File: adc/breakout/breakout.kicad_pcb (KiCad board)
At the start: 2 copper layers, 52 parts, among them J1 Conn_01x05_Pin, J2 Conn_01x05_Pin, J3 Conn_01x03_Pin, J4 Conn_01x06_Pin, U1 ESD5344D-TP, U2 ADS1261IRHBR, U3 ESD5344D-TP, U4 ESD5344D-TP

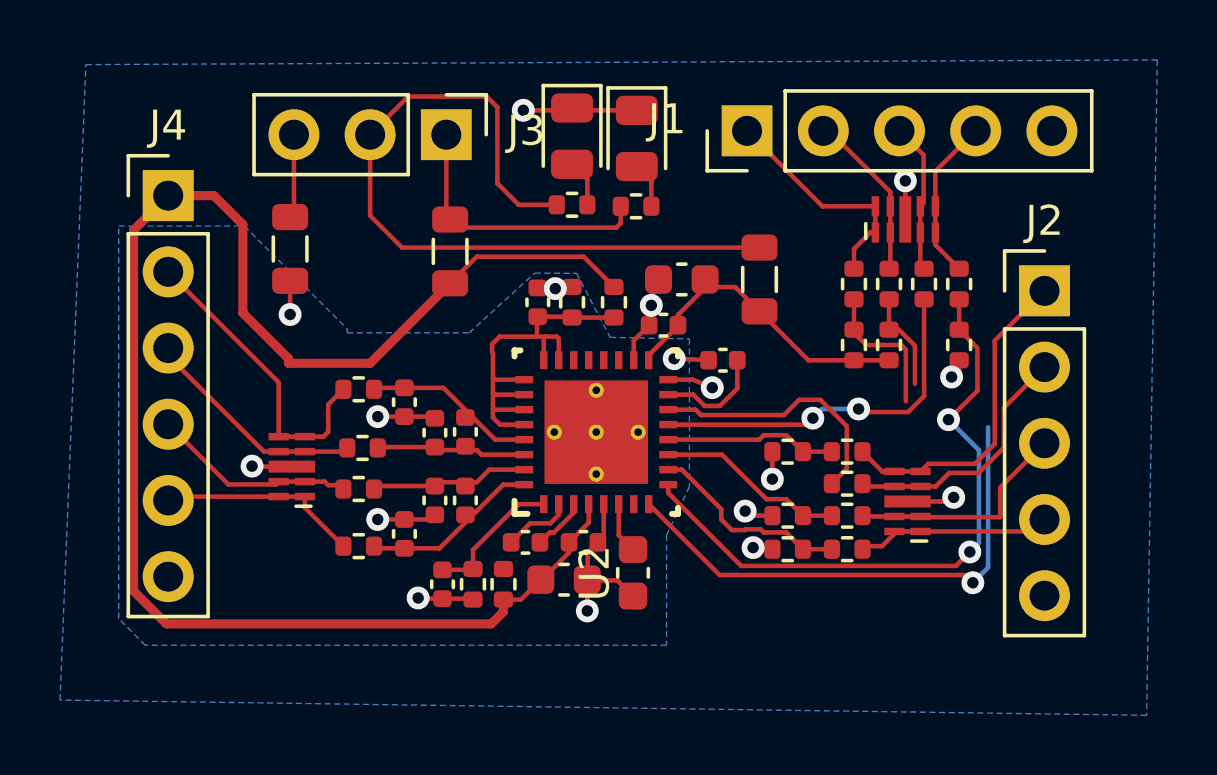
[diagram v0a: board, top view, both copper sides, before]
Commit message: More adc breakout pcb layout cleanup.
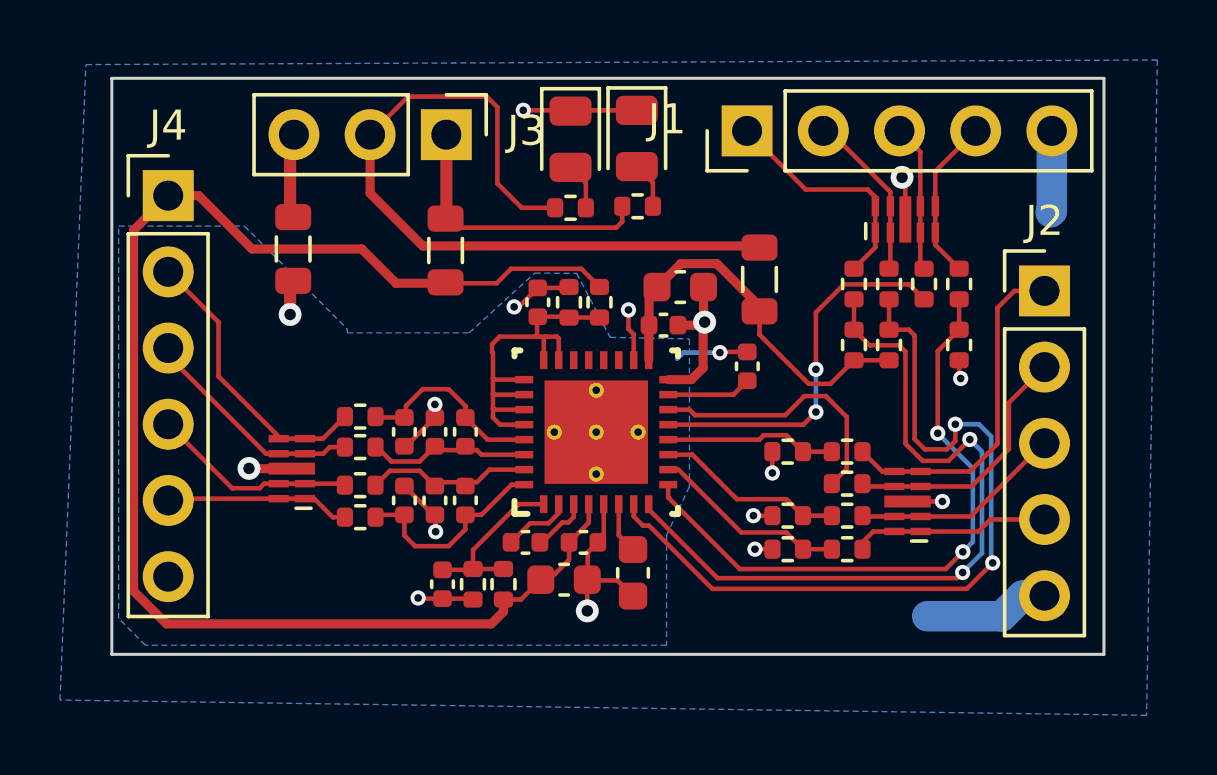
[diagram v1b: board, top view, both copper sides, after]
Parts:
- moved C14 1.11 mm to (113.8, 103.6)
- moved C9 0.99 mm to (113.8, 101.3)
- moved R30 0.97 mm to (112.3, 104.2)
- moved R26 0.91 mm to (112.3, 100.8)
- moved C7 0.84 mm to (125.2, 99.2), turned to 90 degrees
- moved R1 0.48 mm to (120.3, 97.0)
- moved C2 0.26 mm to (123.0, 96.5), turned to 0 degrees
- moved FB3 0.16 mm to (115.2, 95.3)
- moved R29 0.14 mm to (112.3, 103.1)
- moved D2 0.12 mm to (119.3, 91.6)
- moved R22 0.11 mm to (119.3, 93.9)
- moved R3 0.10 mm to (119.3, 97.0)
- moved FB1 0.10 mm to (110.1, 95.2)
- moved R28 0.08 mm to (112.3, 101.9)
- moved U4 0.07 mm to (110.0, 102.6)
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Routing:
- net Net-(U2-PWDN_N): track 3.37 -> 26.9 mm, vias 0 -> 2
- net GNDD: track 17.1 -> 25.3 mm
- net +5VA: track 52.6 -> 47.9 mm
- net Net-(U2-RESET_N): track 22.1 -> 25.3 mm, vias 1 -> 2
- net +3V3: track 10.4 -> 13.1 mm
- net GNDA: track 16.4 -> 17.8 mm
- net /AIN0: track 5.92 -> 6.96 mm
- net Net-(U2-AINCOM): track 4.66 -> 5.67 mm
- net /IN3: track 10.4 -> 9.53 mm
- net Net-(U2-BYPASS): track 3.64 -> 2.83 mm
- net /AIN3: track 5.74 -> 6.51 mm
- net /IN0: track 6.79 -> 6.09 mm
- net Net-(J2-Pin_1): track 10.9 -> 11.5 mm
- net Net-(J2-Pin_2): track 9.27 -> 8.66 mm
- net Net-(J2-Pin_3): track 7.69 -> 7.09 mm
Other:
- board outline added: 33.1 x 19.2 mm

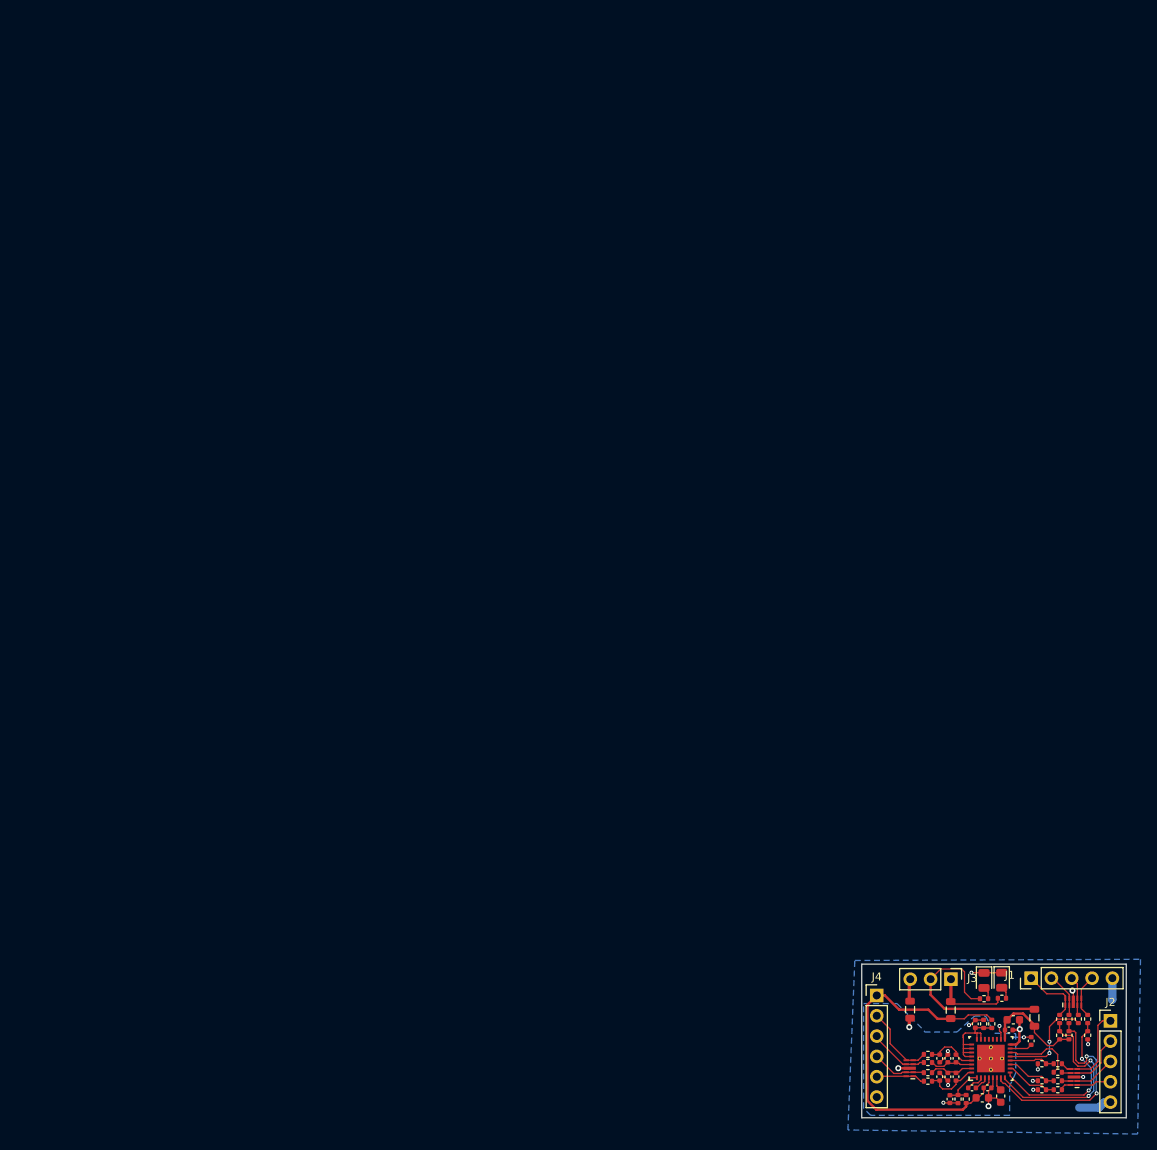
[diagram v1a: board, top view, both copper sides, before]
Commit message: Complete the adc breakout board layout.
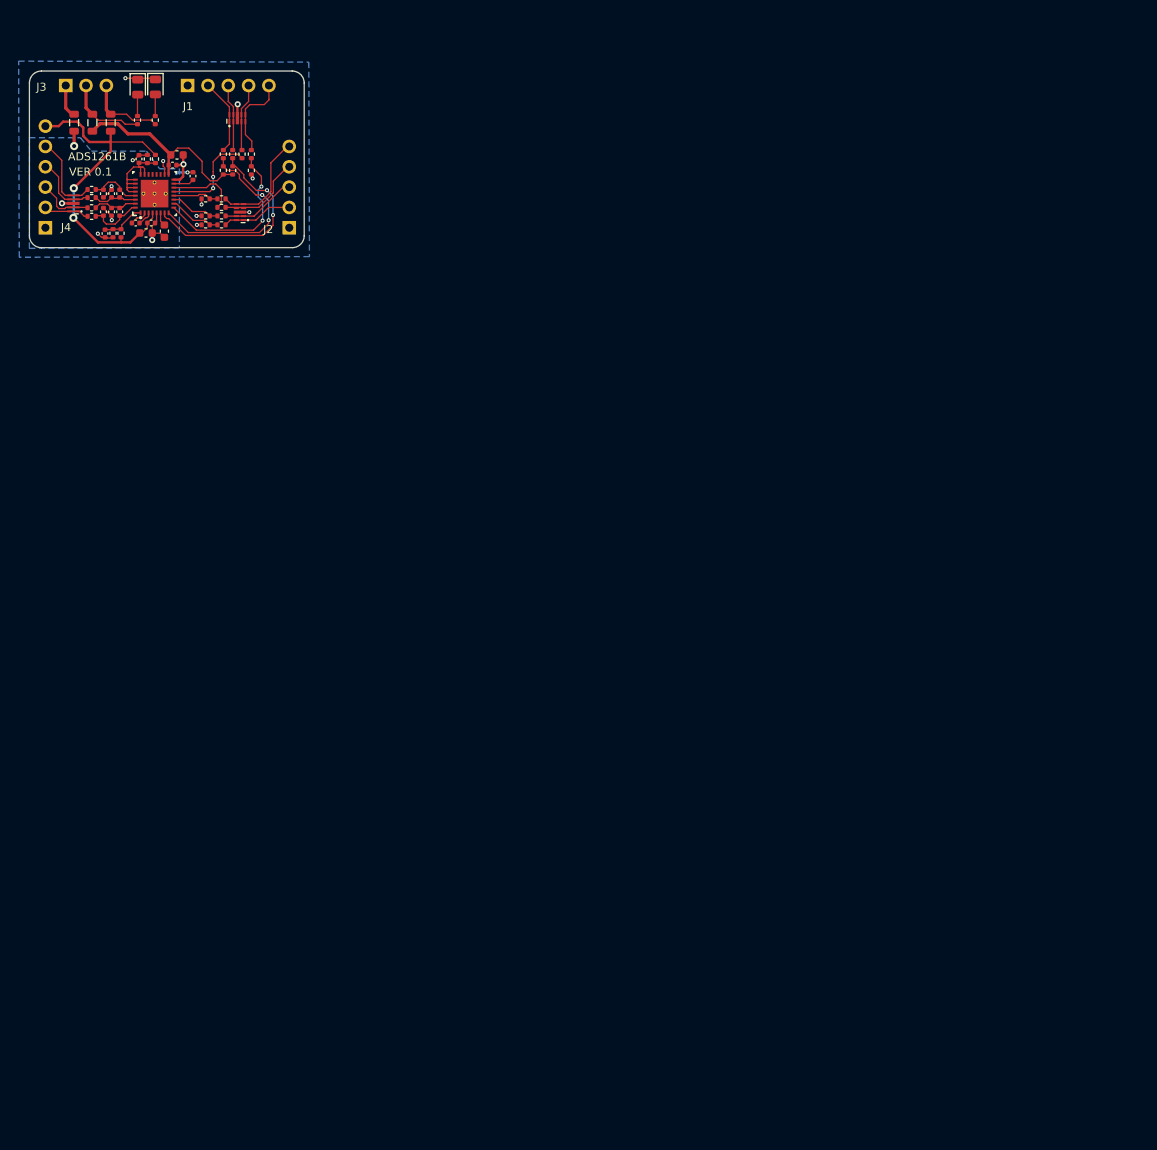
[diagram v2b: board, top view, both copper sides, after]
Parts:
- J1, J2: footprint Connector_PinHeader_2.54mm:PinHeader_1x05_P2.54mm_Vertical -> breakout:PinHeader_1x05_P2.54mm_Vertical
- J3: footprint Connector_PinHeader_2.54mm:PinHeader_1x03_P2.54mm_Vertical -> breakout:PinHeader_1x03_P2.54mm_Vertical
- J4: footprint Connector_PinHeader_2.54mm:PinHeader_1x06_P2.54mm_Vertical -> breakout:PinHeader_1x06_P2.54mm_Vertical
- moved FB2 162.4 mm to (7.87, -15.6)
- moved J3 157.2 mm to (4.54, -20.3), turned to 90 degrees
- moved D1 153.8 mm to (15.8, -20.1)
- moved D2 153.8 mm to (13.5, -20.1)
- moved J1 153.5 mm to (19.8, -20.3)
- moved FB3 152.7 mm to (10.2, -15.6)
- moved R22 152.5 mm to (13.5, -15.9), turned to 90 degrees
- moved R21 152.5 mm to (15.7, -15.9), turned to 90 degrees
- moved FB1 152.4 mm to (5.59, -15.6)
- moved U1 152.0 mm to (26.0, -16.2)
- moved R2 151.2 mm to (11.4, -1.80)
- moved R6 151.2 mm to (10.4, -1.80)
- moved C15 151.2 mm to (9.45, -1.77)
- moved C7 150.6 mm to (20.4, -8.95)
- moved C1 150.4 mm to (14.6, -1.84)
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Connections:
- J1 pad 1: Net-(J1-Pin_1) -> GNDD
- J1 pad 5: GNDD -> Net-(J1-Pin_5)
- J2 pad 1: Net-(J2-Pin_1) -> GNDD
- J2 pad 5: GNDD -> Net-(J2-Pin_5)
- J3 pad 1: /5V_LED -> GNDD
- J3 pad 3: GNDD -> /5V_LED
- J4 pad 1: +5VA -> GNDA
- J4 pad 2: /IN3 -> /IN0
- J4 pad 3: /IN2 -> /IN1
- J4 pad 4: /IN1 -> /IN2
- J4 pad 5: /IN0 -> /IN3
- J4 pad 6: GNDA -> +5VA
- R10 pad 1: Net-(J1-Pin_2) -> Net-(J1-Pin_3)
- R12 pad 1: Net-(J1-Pin_3) -> Net-(J1-Pin_4)
- R14 pad 1: Net-(J1-Pin_4) -> Net-(J1-Pin_5)
- R17 pad 1: Net-(J2-Pin_1) -> Net-(J2-Pin_5)
- R18 pad 1: Net-(J2-Pin_2) -> Net-(J2-Pin_4)
- R20 pad 1: Net-(J2-Pin_4) -> Net-(J2-Pin_2)
- R8 pad 1: Net-(J1-Pin_1) -> Net-(J1-Pin_2)
- U1 pad 1: Net-(J1-Pin_1) -> Net-(J1-Pin_2)
- U1 pad 2: Net-(J1-Pin_2) -> Net-(J1-Pin_3)
- U1 pad 4: Net-(J1-Pin_3) -> Net-(J1-Pin_4)
- U1 pad 5: Net-(J1-Pin_4) -> Net-(J1-Pin_5)
- U3 pad 1: Net-(J2-Pin_4) -> Net-(J2-Pin_2)
- U3 pad 4: Net-(J2-Pin_2) -> Net-(J2-Pin_4)
- U3 pad 5: Net-(J2-Pin_1) -> Net-(J2-Pin_5)
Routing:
- net /3V3_LED: track 25.4 -> 10.1 mm
- net Net-(J2-Pin_5): track 0.00 -> 13.3 mm
- net +3V3: track 13.1 -> 24.9 mm
- net Net-(J2-Pin_1): track 11.5 -> 0.00 mm
- net Net-(J1-Pin_5): track 0.00 -> 10.7 mm
- net Net-(J1-Pin_1): track 7.87 -> 0.00 mm
- net +5VA: track 47.9 -> 42.8 mm, vias 0 -> 2
- net GNDD: track 25.3 -> 20.4 mm
- net Net-(J2-Pin_4): track 6.61 -> 10.9 mm
- net Net-(J1-Pin_2): track 5.66 -> 9.49 mm
- net Net-(J1-Pin_3): track 4.94 -> 8.44 mm
- net Net-(J1-Pin_4): track 5.48 -> 8.65 mm
- net Net-(J2-Pin_3): track 7.09 -> 9.47 mm
- net Net-(D1-A): track 1.54 -> 2.80 mm
- net Net-(D2-A): track 1.56 -> 2.76 mm
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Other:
- board size 33.1 x 19.2 mm -> 34.4 x 22.1 mm
- board text added: "ADS1261B"
- board text added: "VER 0.1"

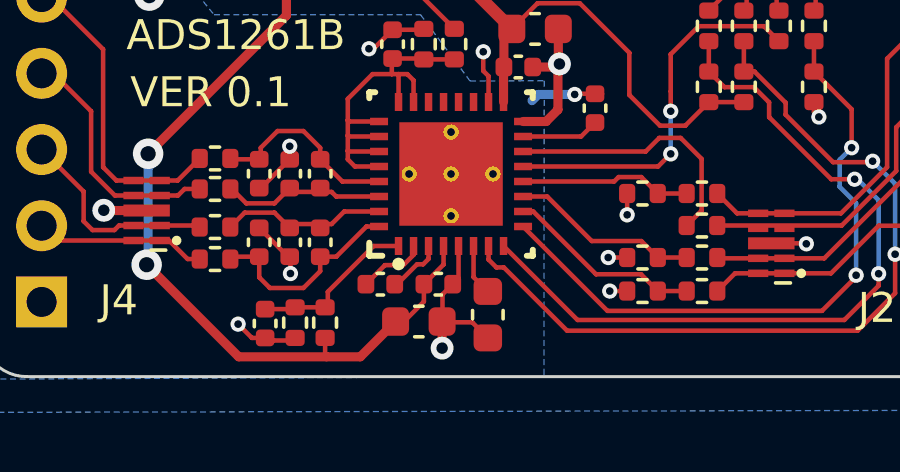
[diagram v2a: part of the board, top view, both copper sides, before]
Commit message: Fixed two component values.
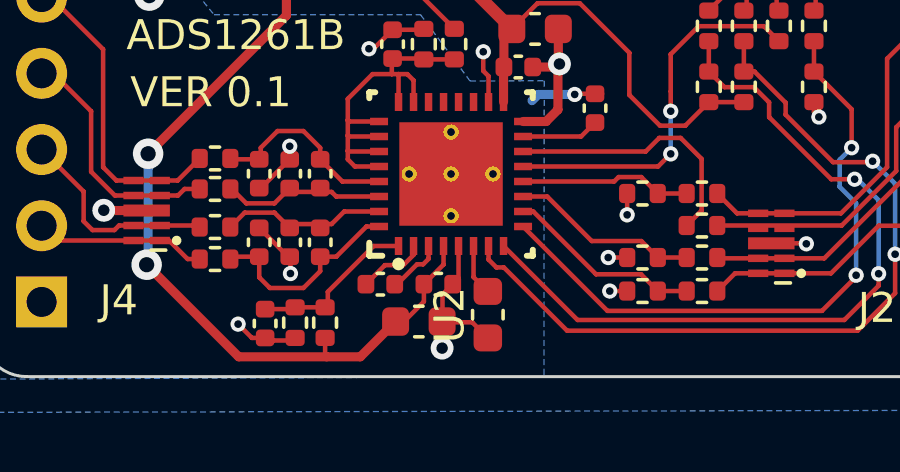
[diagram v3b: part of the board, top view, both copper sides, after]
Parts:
- C6: value 4u7 -> 4n7
- R10, R12, R14, R17, R18, R19, R20, R8: value 100R -> 47R
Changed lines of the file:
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@@
     (descr "Resistor SMD 0402 (1005 Metric), square (rectangular) end terminal, IPC_7351 nominal, (Body size source: IPC-SM-782 page 72, https://www.pcb-3d.com/wordpress/wp-content/uploads/ipc-sm-782a_amendment_1_and_2.pdf), generated with kicad-footprint-generator")
     (tags "resistor")
-    (property "LCSC" "C25076")
+    (property "LCSC" "C25118")
     (property "Sheetfile" "breakout.kicad_sch")
     (property "Sheetname" "")
@@
         (effects (font (size 1 1) (thickness 0.15)))
     )
-    (fp_text value "100R" (at 0 1.17 90) (layer "F.Fab") hide
+    (fp_text value "47R" (at 0 1.17 90) (layer "F.Fab") hide
         (effects (font (size 1 1) (thickness 0.15)))
     )
@@
     (descr "Resistor SMD 0402 (1005 Metric), square (rectangular) end terminal, IPC_7351 nominal, (Body size source: IPC-SM-782 page 72, https://www.pcb-3d.com/wordpress/wp-content/uploads/ipc-sm-782a_amendment_1_and_2.pdf), generated with kicad-footprint-generator")
     (tags "resistor")
-    (property "LCSC" "C25076")
+    (property "LCSC" "C25118")
     (property "Sheetfile" "breakout.kicad_sch")
     (property "Sheetname" "")
@@
         (effects (font (size 1 1) (thickness 0.15)))
     )
-    (fp_text value "100R" (at 0 1.17 90) (layer "F.Fab") hide
+    (fp_text value "47R" (at 0 1.17 90) (layer "F.Fab") hide
         (effects (font (size 1 1) (thickness 0.15)))
     )
@@
     (descr "Resistor SMD 0402 (1005 Metric), square (rectangular) end terminal, IPC_7351 nominal, (Body size source: IPC-SM-782 page 72, https://www.pcb-3d.com/wordpress/wp-content/uploads/ipc-sm-782a_amendment_1_and_2.pdf), generated with kicad-footprint-generator")
     (tags "resistor")
-    (property "LCSC" "C25076")
+    (property "LCSC" "C25118")
     (property "Sheetfile" "breakout.kicad_sch")
     (property "Sheetname" "")
@@
         (effects (font (size 1 1) (thickness 0.15)))
     )
-    (fp_text value "100R" (at 0 1.17) (layer "F.Fab")
+    (fp_text value "47R" (at 0 1.17) (layer "F.Fab")
         (effects (font (size 1 1) (thickness 0.15)))
     )
@@
     (descr "Resistor SMD 0402 (1005 Metric), square (rectangular) end terminal, IPC_7351 nominal, (Body size source: IPC-SM-782 page 72, https://www.pcb-3d.com/wordpress/wp-content/uploads/ipc-sm-782a_amendment_1_and_2.pdf), generated with kicad-footprint-generator")
     (tags "resistor")
-    (property "LCSC" "C25076")
+    (property "LCSC" "C25118")
     (property "Sheetfile" "breakout.kicad_sch")
     (property "Sheetname" "")
@@
         (effects (font (size 1 1) (thickness 0.15)))
     )
-    (fp_text value "100R" (at 0 1.17) (layer "F.Fab")
+    (fp_text value "47R" (at 0 1.17) (layer "F.Fab")
         (effects (font (size 1 1) (thickness 0.15)))
     )
@@
     (descr "Resistor SMD 0402 (1005 Metric), square (rectangular) end terminal, IPC_7351 nominal, (Body size source: IPC-SM-782 page 72, https://www.pcb-3d.com/wordpress/wp-content/uploads/ipc-sm-782a_amendment_1_and_2.pdf), generated with kicad-footprint-generator")
     (tags "resistor")
-    (property "LCSC" "C25076")
+    (property "LCSC" "C25118")
     (property "Sheetfile" "breakout.kicad_sch")
     (property "Sheetname" "")
@@
         (effects (font (size 1 1) (thickness 0.15)))
     )
-    (fp_text value "100R" (at 0 1.17) (layer "F.Fab")
+    (fp_text value "47R" (at 0 1.17) (layer "F.Fab")
         (effects (font (size 1 1) (thickness 0.15)))
     )
@@
     (descr "Resistor SMD 0402 (1005 Metric), square (rectangular) end terminal, IPC_7351 nominal, (Body size source: IPC-SM-782 page 72, https://www.pcb-3d.com/wordpress/wp-content/uploads/ipc-sm-782a_amendment_1_and_2.pdf), generated with kicad-footprint-generator")
     (tags "resistor")
-    (property "LCSC" "C25076")
+    (property "LCSC" "C25118")
     (property "Sheetfile" "breakout.kicad_sch")
     (property "Sheetname" "")
@@
         (effects (font (size 1 1) (thickness 0.15)))
     )
-    (fp_text value "100R" (at 0 1.17) (layer "F.Fab")
+    (fp_text value "47R" (at 0 1.17) (layer "F.Fab")
         (effects (font (size 1 1) (thickness 0.15)))
     )
@@
     (descr "Resistor SMD 0402 (1005 Metric), square (rectangular) end terminal, IPC_7351 nominal, (Body size source: IPC-SM-782 page 72, https://www.pcb-3d.com/wordpress/wp-content/uploads/ipc-sm-782a_amendment_1_and_2.pdf), generated with kicad-footprint-generator")
     (tags "resistor")
-    (property "LCSC" "C25076")
+    (property "LCSC" "C25118")
     (property "Sheetfile" "breakout.kicad_sch")
     (property "Sheetname" "")
@@
         (effects (font (size 1 1) (thickness 0.15)))
     )
-    (fp_text value "100R" (at 0 1.17 90) (layer "F.Fab") hide
+    (fp_text value "47R" (at 0 1.17 90) (layer "F.Fab") hide
         (effects (font (size 1 1) (thickness 0.15)))
     )
@@
     (descr "Capacitor SMD 0402 (1005 Metric), square (rectangular) end terminal, IPC_7351 nominal, (Body size source: IPC-SM-782 page 76, https://www.pcb-3d.com/wordpress/wp-content/uploads/ipc-sm-782a_amendment_1_and_2.pdf), generated with kicad-footprint-generator")
     (tags "capacitor")
-    (property "LCSC" "C23733")
+    (property "LCSC" "C1538")
     (property "Sheetfile" "breakout.kicad_sch")
     (property "Sheetname" "")
@@
         (effects (font (size 1 1) (thickness 0.15)))
     )
-    (fp_text value "4u7" (at 0 1.16) (layer "F.Fab")
+    (fp_text value "4n7" (at 0 1.16) (layer "F.Fab")
         (effects (font (size 1 1) (thickness 0.15)))
     )
@@
     (descr "Resistor SMD 0402 (1005 Metric), square (rectangular) end terminal, IPC_7351 nominal, (Body size source: IPC-SM-782 page 72, https://www.pcb-3d.com/wordpress/wp-content/uploads/ipc-sm-782a_amendment_1_and_2.pdf), generated with kicad-footprint-generator")
     (tags "resistor")
-    (property "LCSC" "C25076")
+    (property "LCSC" "C25118")
     (property "Sheetfile" "breakout.kicad_sch")
     (property "Sheetname" "")
@@
         (effects (font (size 1 1) (thickness 0.15)))
     )
-    (fp_text value "100R" (at 0 1.17 90) (layer "F.Fab") hide
+    (fp_text value "47R" (at 0 1.17 90) (layer "F.Fab") hide
         (effects (font (size 1 1) (thickness 0.15)))
     )
@@
     (property "ki_keywords" "ADS1261IRHBR")
     (attr smd)
-    (fp_text reference "U2" (at -4.7 -0.05 90 unlocked) (layer "F.SilkS") hide
-        (effects (font (size 1 1) (thickness 0.15)))
-    )
+    (fp_text reference "U2" (at -4.7 -0.05 90 unlocked) (layer "F.SilkS")
+        (effects (font (size 1 1) (thickness 0.15)))
+    )
